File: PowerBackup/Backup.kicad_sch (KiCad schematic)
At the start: 4 parts, among them J7 Conn_01x02_Male

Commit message: Trying things
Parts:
- removed D1, D2: MBRB2515L, Package_TO_SOT_SMD:TO-263-2, symbol Device:D_Schottky_AKA
- added D1, D2: SB2060TA, Diode_THT:D_A-405_P5.08mm_Vertical_KathodeUp, symbol Device:D_Schottky
- added J10, J8, J9: Conn_01x02_Female, Connector_JST:JST_XH_B2B-XH-A_1x02_P2.50mm_Vertical, symbol Connector:Conn_01x02_Female
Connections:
- net +9V: now also D1.2 (A)
- net +9VA: now also D1.1 (K), D2.1 (K)
- net VBAT: now also D2.2 (A)
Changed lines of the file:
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@@
 (kicad_sch (version 20211123) (generator eeschema)
   (paper "A4")
-  (junction (at 56.134 47.498) (diameter 0) (color 0 0 0 0)
-  )
-  (junction (at 56.134 39.37) (diameter 0) (color 0 0 0 0)
-  )
   (junction (at 65.024 43.434) (diameter 0) (color 0 0 0 0)
   )
@@
     (stroke (width 0) (type default) (color 0 0 0 0))
   )
+  (wire (pts (xy 63.754 47.498) (xy 65.024 47.498))
+    (stroke (width 0) (type default) (color 0 0 0 0))
+  )
   (wire (pts (xy 37.846 47.498) (xy 56.134 47.498))
     (stroke (width 0) (type default) (color 0 0 0 0))
@@
     (stroke (width 0) (type default) (color 0 0 0 0))
   )
+  (wire (pts (xy 63.754 39.37) (xy 65.024 39.37))
+    (stroke (width 0) (type default) (color 0 0 0 0))
+  )
   (wire (pts (xy 65.024 43.434) (xy 65.024 47.498))
     (stroke (width 0) (type default) (color 0 0 0 0))
   )
   (wire (pts (xy 37.846 50.038) (xy 37.846 51.562))
-    (stroke (width 0) (type default) (color 0 0 0 0))
-  )
-  (wire (pts (xy 56.134 50.038) (xy 56.134 47.498))
-    (stroke (width 0) (type default) (color 0 0 0 0))
-  )
-  (wire (pts (xy 56.134 41.91) (xy 56.134 39.37))
     (stroke (width 0) (type default) (color 0 0 0 0))
   )
@@
     (effects (font (size 1.27 1.27)) (justify left bottom))
   )
+  (symbol (lib_id "Device:D_Schottky") (at 59.944 39.37 180) (unit 1)
+    (in_bom yes) (on_board yes) (fields_autoplaced)
+    (property "Reference" "D1" (id 0) (at 60.2615 33.02 0))
+    (property "Value" "SB2060TA" (id 1) (at 60.2615 35.56 0))
+    (property "Footprint" "Diode_THT:D_A-405_P5.08mm_Vertical_KathodeUp" (id 2) (at 59.944 39.37 0)
+      (effects (font (size 1.27 1.27)) hide)
+    )
+    (property "Datasheet" "http://www.smc-diodes.com/propdf/SB2060%20N0876%20REV.A.pdf" (id 3) (at 59.944 39.37 0)
+      (effects (font (size 1.27 1.27)) hide)
+    )
+    (pin "1")
+    (pin "2")
+  )
+  (symbol (lib_id "Connector:Conn_01x02_Female") (at 242.57 79.502 0) (unit 1)
+    (in_bom yes) (on_board yes) (fields_autoplaced)
+    (property "Reference" "J10" (id 0) (at 243.84 79.5019 0)
+      (effects (font (size 1.27 1.27)) (justify left))
+    )
+    (property "Value" "Conn_01x02_Female" (id 1) (at 243.84 82.0419 0)
+      (effects (font (size 1.27 1.27)) (justify left))
+    )
+    (property "Footprint" "Connector_JST:JST_XH_B2B-XH-A_1x02_P2.50mm_Vertical" (id 2) (at 242.57 79.502 0)
+      (effects (font (size 1.27 1.27)) hide)
+    )
+    (property "Datasheet" "~" (id 3) (at 242.57 79.502 0)
+      (effects (font (size 1.27 1.27)) hide)
+    )
+    (pin "1")
+    (pin "2")
+  )
+  (symbol (lib_id "Connector:Conn_01x02_Female") (at 242.316 63.5 0) (unit 1)
+    (in_bom yes) (on_board yes) (fields_autoplaced)
+    (property "Reference" "J8" (id 0) (at 243.84 63.4999 0)
+      (effects (font (size 1.27 1.27)) (justify left))
+    )
+    (property "Value" "Conn_01x02_Female" (id 1) (at 243.84 66.0399 0)
+      (effects (font (size 1.27 1.27)) (justify left))
+    )
+    (property "Footprint" "Connector_JST:JST_XH_B2B-XH-A_1x02_P2.50mm_Vertical" (id 2) (at 242.316 63.5 0)
+      (effects (font (size 1.27 1.27)) hide)
+    )
+    (property "Datasheet" "~" (id 3) (at 242.316 63.5 0)
+      (effects (font (size 1.27 1.27)) hide)
+    )
+    (pin "1")
+    (pin "2")
+  )
+  (symbol (lib_id "Connector:Conn_01x02_Female") (at 242.57 48.768 0) (unit 1)
+    (in_bom yes) (on_board yes) (fields_autoplaced)
+    (property "Reference" "J9" (id 0) (at 243.84 48.7679 0)
+      (effects (font (size 1.27 1.27)) (justify left))
+    )
+    (property "Value" "Conn_01x02_Female" (id 1) (at 243.84 51.3079 0)
+      (effects (font (size 1.27 1.27)) (justify left))
+    )
+    (property "Footprint" "Connector_JST:JST_XH_B2B-XH-A_1x02_P2.50mm_Vertical" (id 2) (at 242.57 48.768 0)
+      (effects (font (size 1.27 1.27)) hide)
+    )
+    (property "Datasheet" "~" (id 3) (at 242.57 48.768 0)
+      (effects (font (size 1.27 1.27)) hide)
+    )
+    (pin "1")
+    (pin "2")
+  )
   (symbol (lib_id "Device:C_Small") (at 72.644 45.974 0) (unit 1)
     (in_bom yes) (on_board yes) (fields_autoplaced)
@@
     (pin "1")
   )
-  (symbol (lib_id "Device:D_Schottky_AKA") (at 61.214 39.37 180) (unit 1)
-    (in_bom yes) (on_board yes) (fields_autoplaced)
-    (property "Reference" "D1" (id 0) (at 60.325 32.766 0))
-    (property "Value" "MBRB2515L" (id 1) (at 60.325 35.306 0))
-    (property "Footprint" "Package_TO_SOT_SMD:TO-263-2" (id 2) (at 61.214 39.37 0)
-      (effects (font (size 1.27 1.27)) hide)
-    )
-    (property "Datasheet" "~https://www.onsemi.com/pdf/datasheet/mbrb2515l-d.pdf" (id 3) (at 61.214 39.37 0)
-      (effects (font (size 1.27 1.27)) hide)
-    )
-    (pin "1")
-    (pin "2")
-    (pin "3")
-  )
   (symbol (lib_id "power:+9VA") (at 72.644 42.164 0) (unit 1)
     (in_bom yes) (on_board yes) (fields_autoplaced)
@@
     )
     (pin "1")
+  )
+  (symbol (lib_id "Device:D_Schottky") (at 59.944 47.498 180) (unit 1)
+    (in_bom yes) (on_board yes)
+    (property "Reference" "D2" (id 0) (at 59.182 42.672 0))
+    (property "Value" "SB2060TA" (id 1) (at 57.912 44.704 0))
+    (property "Footprint" "Diode_THT:D_A-405_P5.08mm_Vertical_KathodeUp" (id 2) (at 59.944 47.498 0)
+      (effects (font (size 1.27 1.27)) hide)
+    )
+    (property "Datasheet" "http://www.smc-diodes.com/propdf/SB2060%20N0876%20REV.A.pdf" (id 3) (at 59.944 47.498 0)
+      (effects (font (size 1.27 1.27)) hide)
+    )
+    (pin "1")
+    (pin "2")
   )
   (symbol (lib_id "Connector:Conn_01x02_Male") (at 32.766 47.498 0) (unit 1)
@@
     (pin "2")
   )
-  (symbol (lib_id "Device:D_Schottky_AKA") (at 61.214 47.498 180) (unit 1)
-    (in_bom yes) (on_board yes)
-    (property "Reference" "D2" (id 0) (at 61.214 50.292 0))
-    (property "Value" "MBRB2515L" (id 1) (at 62.23 53.34 0))
-    (property "Footprint" "Package_TO_SOT_SMD:TO-263-2" (id 2) (at 61.214 47.498 0)
-      (effects (font (size 1.27 1.27)) hide)
-    )
-    (property "Datasheet" "~https://www.onsemi.com/pdf/datasheet/mbrb2515l-d.pdf" (id 3) (at 61.214 47.498 0)
-      (effects (font (size 1.27 1.27)) hide)
-    )
-    (pin "1")
-    (pin "2")
-    (pin "3")
-  )
 )

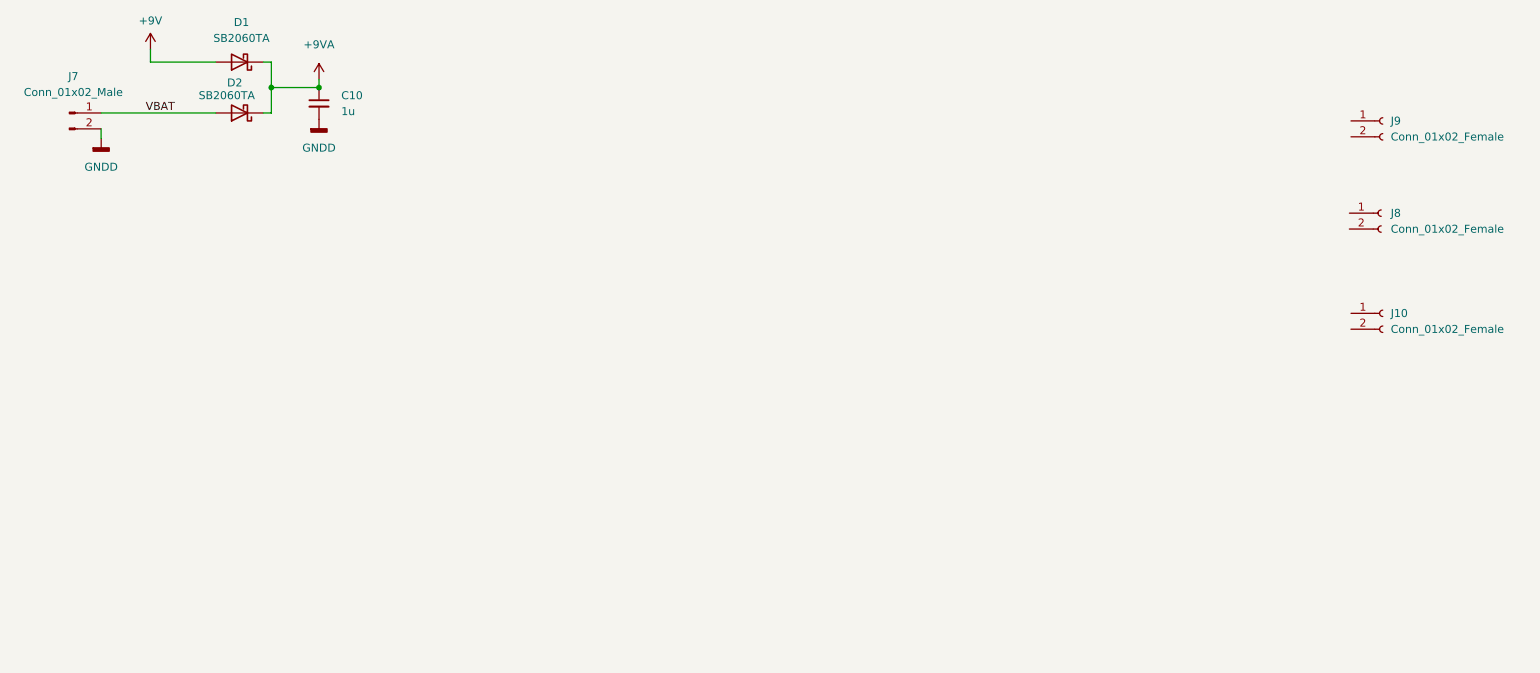
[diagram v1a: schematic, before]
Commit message: Adding regulator
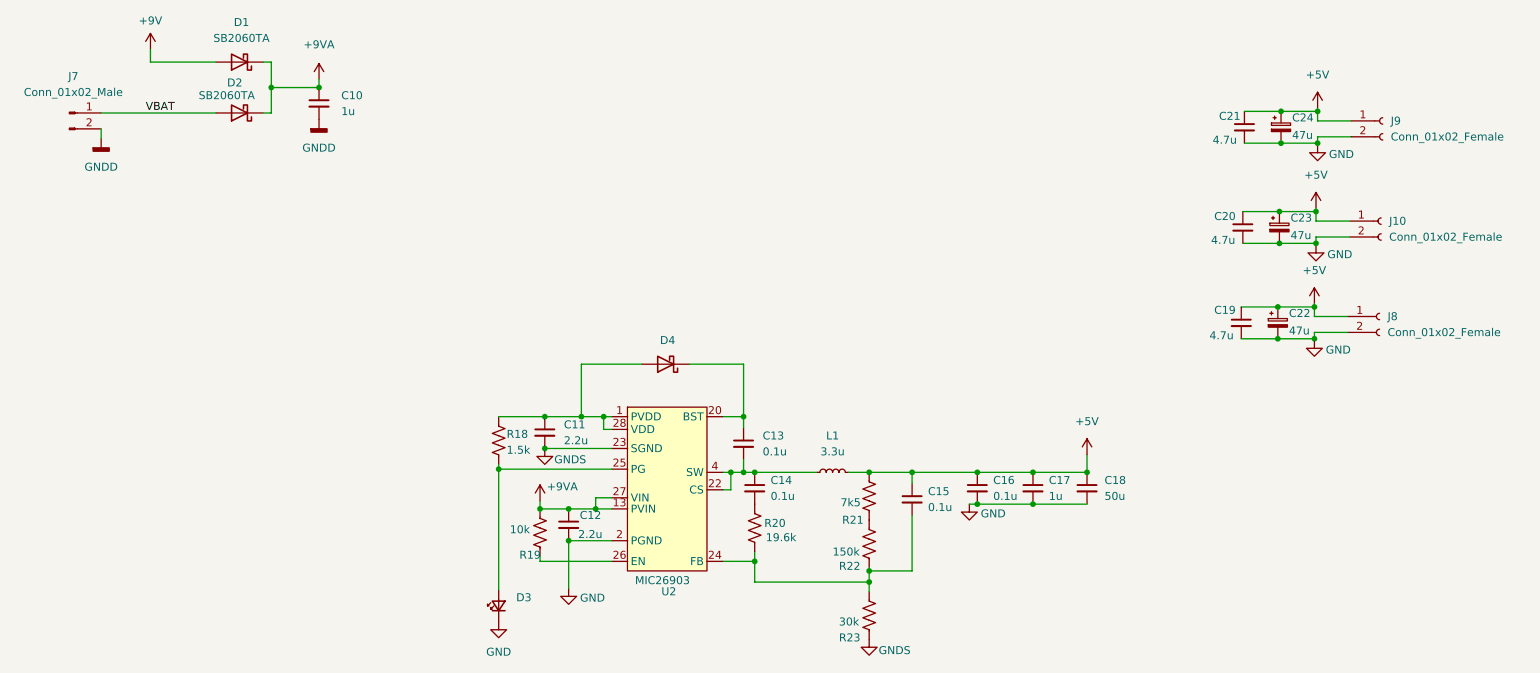
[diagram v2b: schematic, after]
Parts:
- added C11, C12: 2.2u, symbol Device:C_Small
- added C13, C14, C15, C16: 0.1u, symbol Device:C_Small
- added C17: 1u, symbol Device:C_Small
- added C18: 50u, symbol Device:C_Small
- added C19, C20, C21: 4.7u, symbol Device:C_Small
- added C22, C23, C24: 47u, symbol Device:C_Polarized_Small
- added D3: LED_Small, symbol Device:LED_Small
- added D4: BAT54HMFHT116, symbol Device:D_Schottky
- added L1: 3.3u, symbol Device:L_Small
- added R18: 1.5k, symbol Device:R_US
- added R19: 10k, symbol Device:R_US
- added R20: 19.6k, symbol Device:R_US
- added R21: 7k5, symbol Device:R_US
- added R22: 150k, symbol Device:R_US
- added R23: 30k, symbol Device:R_US
- added U2: MIC26903, symbol PowerBackup:MIC26903
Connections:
- net +9VA: now also C12.1, R19.1, U2.13 (PVIN), U2.14 (PVIN), U2.15 (PVIN), U2.16 (PVIN), U2.17 (PVIN), U2.18 (PVIN), U2.19 (PVIN), U2.27 (VIN)
- net +5V: now reaches J10.1 (Pin_1)
- net +5V: now also J8.1 (Pin_1), J9.1 (Pin_1), C15.1, C16.1, C17.1, C18.1, C19.1, C20.1, C21.1, C22.1, C23.1, C24.1, L1.2, R21.1
- net GND: now reaches J10.2 (Pin_2)
- net GND: now also J8.2 (Pin_2), J9.2 (Pin_2), C12.2, C16.2, C17.2, C18.2, C19.2, C20.2, C21.2, C22.2, C23.2, C24.2, D3.1 (K), U2.2 (PGND), U2.21 (PGND), U2.5 (PGND), U2.6 (PGND), U2.7 (PGND), U2.8 (PGND)
- new net: D3.2 (A), R18.2, U2.25 (PG)
- new net: R21.2, R22.1
- new net: C13.2, C14.1, L1.1, U2.10 (SW), U2.11 (SW), U2.12 (SW), U2.22 (CS), U2.4 (SW), U2.9 (SW)
- new net: C13.1, D4.1 (K), U2.20 (BST)
- new net: C11.1, D4.2 (A), R18.1, U2.1 (PVDD), U2.28 (VDD)
- new net: C15.2, R20.2, R22.2, R23.1, U2.24 (FB)
- new net: R19.2, U2.26 (EN)
- new net: C14.2, R20.1
- new net GNDS: C11.2, R23.2, U2.23 (SGND)

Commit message: Added 5V 9A buck converter
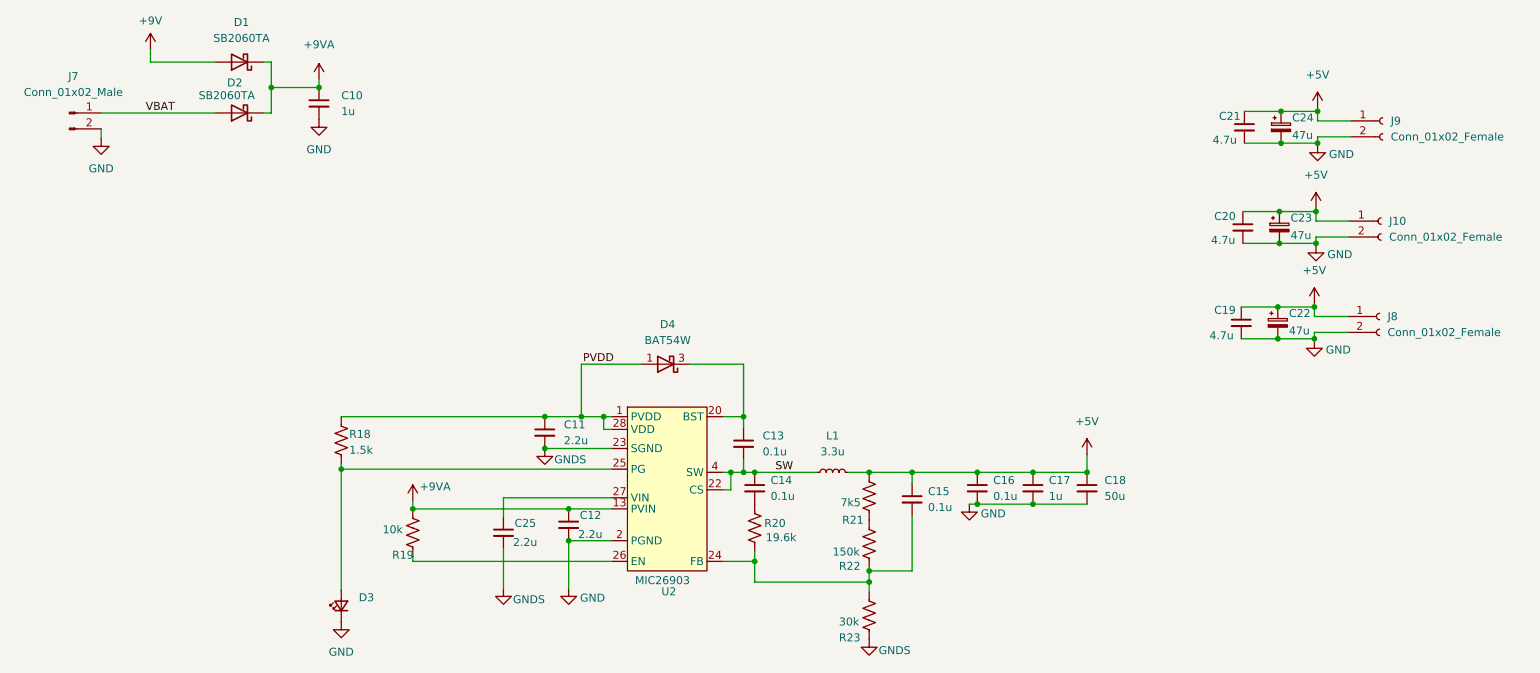
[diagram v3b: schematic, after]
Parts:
- removed D4: BAT54HMFHT116, symbol Device:D_Schottky
- added C25: 2.2u, Capacitor_SMD:C_0603_1608Metric, symbol Device:C_Small
- added D4: BAT54W, Package_TO_SOT_SMD:SOT-323_SC-70, symbol Diode:BAT54W
- C10: footprint Capacitor_SMD:C_0805_2012Metric -> Capacitor_SMD:C_0603_1608Metric
- C11, C12, C13, C14, C15, C16, C17, C18, C19, C20, C21: footprint (none) -> Capacitor_SMD:C_0603_1608Metric
- C22, C23, C24: footprint (none) -> Capacitor_Tantalum_SMD:CP_EIA-6032-15_Kemet-U
- D3: footprint (none) -> LED_SMD:LED_0805_2012Metric
- L1: footprint (none) -> Backup:Inductor_EXL1V0707-3R3-R
- R18, R19, R20, R21, R22, R23: footprint (none) -> Resistor_SMD:R_0603_1608Metric
- U2: footprint (none) -> Backup:MIC26903YJL-TR
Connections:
- net GNDD is gone; now on net GND: C10.2, J7.2 (Pin_2)
- net +9VA: no longer U2.27 (VIN)
- net GNDS: now also C25.2
- net SW: now reaches C13.2, C14.1, L1.1, U2.10 (SW), U2.11 (SW), U2.12 (SW), U2.22 (CS), U2.4 (SW), U2.9 (SW)
- net at C13.1, U2.20 (BST): now also D4.3 (K)
- net PVDD: now reaches C11.1, R18.1, U2.1 (PVDD), U2.28 (VDD)
- net PVDD: now also D4.1 (A)
- new net: C25.1, U2.27 (VIN)
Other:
- moved on the sheet: D3, R18, R19

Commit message: Looking over desing
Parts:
- removed C18: 50u, Capacitor_SMD:C_0603_1608Metric, symbol Device:C_Small
- added C18: 47u, Capacitor_Tantalum_SMD:CP_EIA-6032-15_Kemet-U, symbol Device:C_Polarized_Small
- R20: value 19.6k -> 10k
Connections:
- net +5V: now also C18.1
- net GND: now also C18.2
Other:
- note added: "Inductor Current: Calculated: 9.73A Chosen rated: 15A"
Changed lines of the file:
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@@
   (junction (at 231.648 83.566) (diameter 0) (color 0 0 0 0)
   )
+  (junction (at 142.24 119.126) (diameter 0) (color 0 0 0 0)
+  )
+  (junction (at 231.648 78.486) (diameter 0) (color 0 0 0 0)
+  )
+  (junction (at 226.314 52.324) (diameter 0) (color 0 0 0 0)
+  )
+  (junction (at 76.2 104.394) (diameter 0) (color 0 0 0 0)
+  )
+  (junction (at 87.63 110.744) (diameter 0) (color 0 0 0 0)
+  )
+  (junction (at 225.806 78.486) (diameter 0) (color 0 0 0 0)
+  )
   (junction (at 195.326 104.902) (diameter 0) (color 0 0 0 0)
   )
-  (junction (at 142.24 119.126) (diameter 0) (color 0 0 0 0)
-  )
-  (junction (at 231.648 78.486) (diameter 0) (color 0 0 0 0)
-  )
-  (junction (at 226.314 52.324) (diameter 0) (color 0 0 0 0)
-  )
-  (junction (at 76.2 104.394) (diameter 0) (color 0 0 0 0)
-  )
-  (junction (at 87.63 110.744) (diameter 0) (color 0 0 0 0)
-  )
-  (junction (at 225.806 78.486) (diameter 0) (color 0 0 0 0)
-  )
   (junction (at 108.712 101.092) (diameter 0) (color 0 0 0 0)
   )
@@
   (wire (pts (xy 87.63 119.126) (xy 119.38 119.126))
     (stroke (width 0) (type default) (color 0 0 0 0))
+  )
+  (text "Inductor Current:\nCalculated: 9.73A\nChosen rated: 15A"
+    (at 149.352 96.266 0)
+    (effects (font (size 1.27 1.27)) (justify left bottom))
   )
   (label "VBAT" (at 44.958 47.498 0)
@@
     (pin "2")
   )
+  (symbol (lib_id "Device:C_Polarized_Small") (at 195.326 107.442 0) (unit 1)
+    (in_bom yes) (on_board yes)
+    (property "Reference" "C18" (id 0) (at 197.104 105.918 0)
+      (effects (font (size 1.27 1.27)) (justify left))
+    )
+    (property "Value" "47u" (id 1) (at 197.104 108.712 0)
+      (effects (font (size 1.27 1.27)) (justify left))
+    )
+    (property "Footprint" "Capacitor_Tantalum_SMD:CP_EIA-6032-15_Kemet-U" (id 2) (at 195.326 107.442 0)
+      (effects (font (size 1.27 1.27)) hide)
+    )
+    (property "Datasheet" "~" (id 3) (at 195.326 107.442 0)
+      (effects (font (size 1.27 1.27)) hide)
+    )
+    (pin "1")
+    (pin "2")
+  )
   (symbol (lib_id "power:GND") (at 231.648 83.82 0) (unit 1)
     (in_bom yes) (on_board yes)
@@
       (effects (font (size 1.27 1.27)) (justify left))
     )
-    (property "Value" "19.6k" (id 1) (at 144.018 115.316 0)
+    (property "Value" "10k" (id 1) (at 144.018 115.316 0)
       (effects (font (size 1.27 1.27)) (justify left))
     )
@@
       (effects (font (size 1.27 1.27)) hide)
     )
-    (pin "1")
-    (pin "2")
-  )
-  (symbol (lib_id "Device:C_Small") (at 195.326 107.442 0) (unit 1)
-    (in_bom yes) (on_board yes) (fields_autoplaced)
-    (property "Reference" "C18" (id 0) (at 198.12 106.1782 0)
-      (effects (font (size 1.27 1.27)) (justify left))
-    )
-    (property "Value" "50u" (id 1) (at 198.12 108.7182 0)
-      (effects (font (size 1.27 1.27)) (justify left))
-    )
-    (property "Footprint" "Capacitor_SMD:C_0603_1608Metric" (id 2) (at 195.326 107.442 0)
-      (effects (font (size 1.27 1.27)) hide)
-    )
-    (property "Datasheet" "~" (id 3) (at 195.326 107.442 0)
-      (effects (font (size 1.27 1.27)) hide)
-    )

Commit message: Added BOM and production files
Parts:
- C10, C17: MFN# (none) -> C1608X6S1H105K080AC
- C11, C12, C25: MFN# (none) -> GRM188C71E225KE11D
- C13, C14, C15, C16: MFN# (none) -> TMK107BBJ475MA-T
- C18, C22, C23, C24: MFN# (none) -> TAJC476K010RNJ
- C19, C20, C21: MFN# (none) -> CL10A475KP8NNNC
- D1, D2: MFN# (none) -> SB2060TA
- D3: MFN# (none) -> 150080VS75000
- D4: MFN# (none) -> BAT54W,115
- J10, J7, J8, J9: MFN# (none) -> -
- R18: value 1.5k -> 1k; MFN# (none) -> RNCP0603FTD10K0
- R19, R20: MFN# (none) -> RNCP0603FTD10K0
- R21: MFN# (none) -> RMCF0603FT7K50
- R22: MFN# (none) -> CRGCQ0603F150K
- R23: MFN# (none) -> WR06X1003FTL
- U2: MFN# (none) -> MIC26903YJL-TR
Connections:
- net GNDS is gone; now on net GND: C11.2, C25.2, R23.2, U2.23 (SGND)

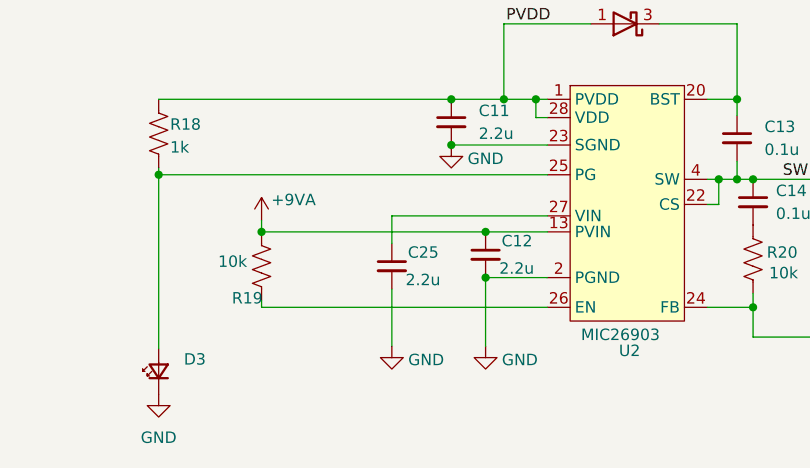
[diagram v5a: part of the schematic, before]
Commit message: Pvin is connected to Vin through a 2.21R resistor
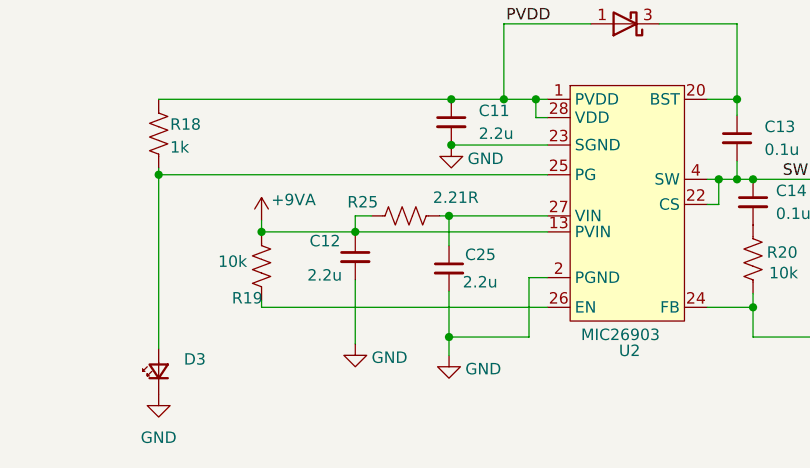
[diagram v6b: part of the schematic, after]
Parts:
- added R25: 2.21R, Resistor_SMD:R_0603_1608Metric, symbol Device:R_US
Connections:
- net +9VA: now also R25.1
- net at C25.1, U2.27 (VIN): now also R25.2
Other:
- moved on the sheet: C12, C25

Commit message: Commiting before order, Regenerated gerbers for both boards
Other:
- moved on the sheet: C11, C12, C13, C14, C15, C16, C17, C18, C25, D3, D4, L1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
